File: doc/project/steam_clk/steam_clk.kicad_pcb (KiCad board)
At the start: 2 copper layers, 53.8 x 35.1 mm, 24 parts, among them J1 Goldpin, J2 Cell+, J3 Cell-, SW1 POWER, SW2 SET, SW3 CLEAR, U1 BQ-M322RD, U2 STM32F030F4Px, U3 TC1185-3.3VCT8, Y1 18.432MHz

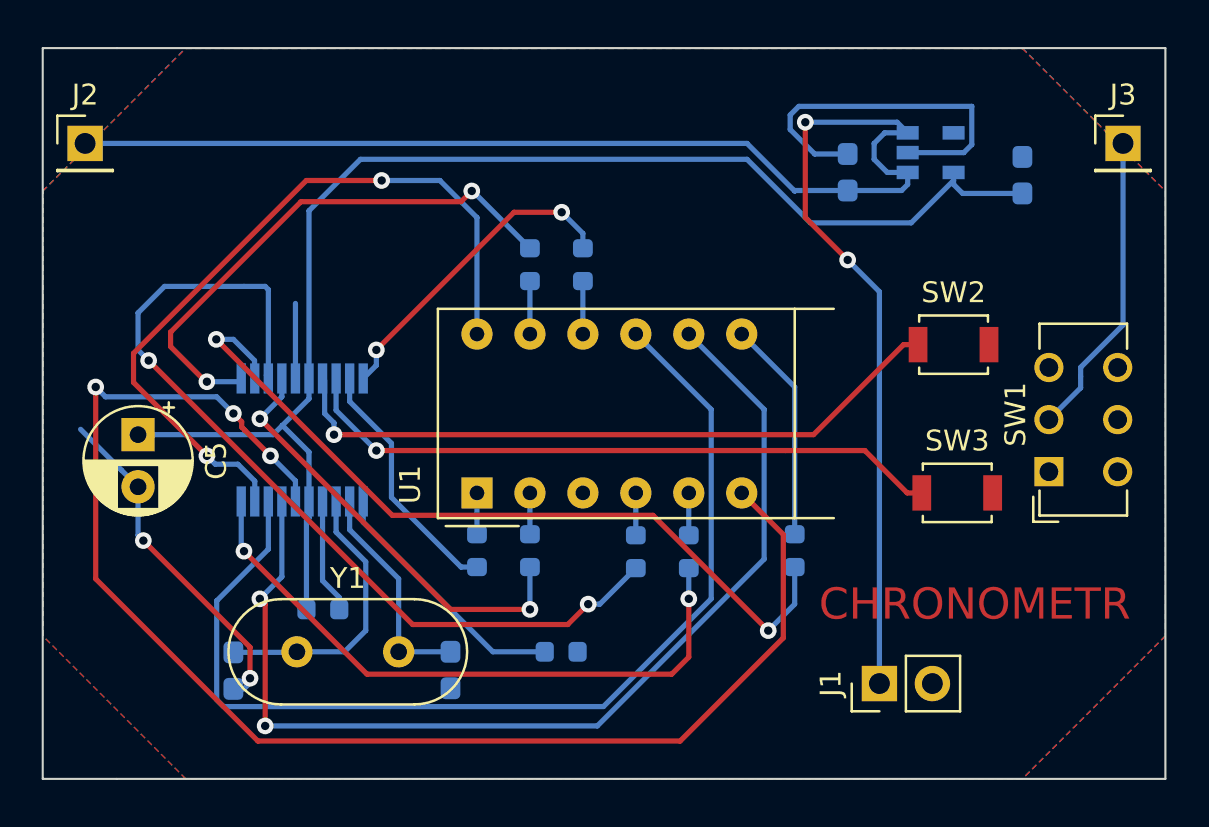
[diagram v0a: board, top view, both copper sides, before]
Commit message: better tracks on pcb
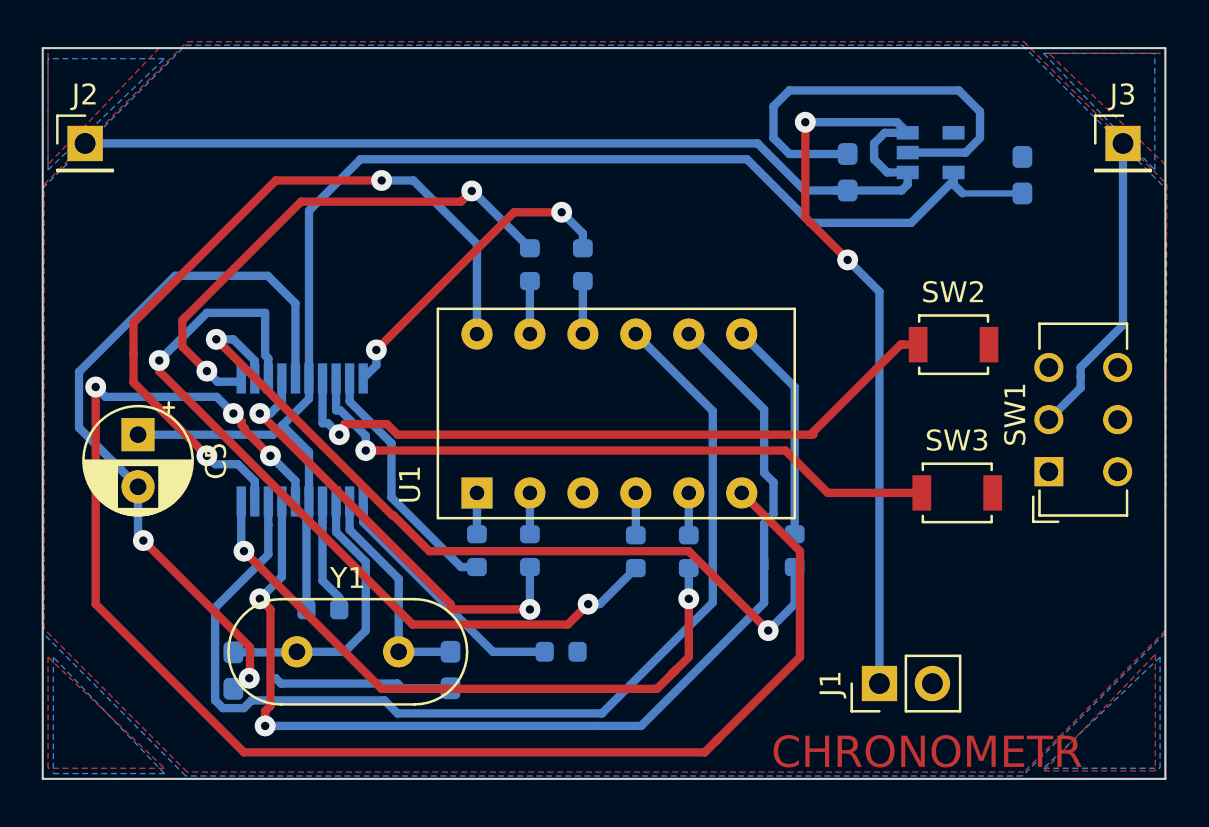
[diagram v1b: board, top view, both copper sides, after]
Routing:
- net GND: track 38.0 -> 65.8 mm
- net SC: track 43.2 -> 38.8 mm
- net D4: track 67.8 -> 70.8 mm
- net D3: track 50.4 -> 53.0 mm
- net D2: track 50.3 -> 51.6 mm
- net SG: track 30.8 -> 31.7 mm
- net Net-(SW2-Pad1): track 32.7 -> 33.4 mm
- net SA: track 25.8 -> 25.2 mm
- net Net-(C1-Pad1): track 11.3 -> 10.7 mm
- added copper zone on B.Cu, net (none)
- added copper zone on F.Cu, net (none)
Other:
- net class +3V3 added: clearance 0.2, trace_width 0.6, via_dia 1, via_drill 0.4
- net class Default: trace_width 0.25 -> 0.4; via_dia 0.8 -> 1
- net class GND added: clearance 0.2, trace_width 0.6, via_dia 1, via_drill 0.4
- rule trace_min: 0.2 -> 0.3
